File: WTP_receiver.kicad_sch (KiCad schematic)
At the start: 14 parts, among them J1 Conn_01x01_Male, J2 Conn_01x01_Male

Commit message: initial version with traces and components
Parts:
- added C10, C11, C12, C13, C14, C7, C8, C9: C, Capacitor_SMD:C_1111_2828_metric, symbol Device:C
- added C5: 10uF, Capacitor_SMD:C_1210_3225Metric, symbol Device:C
- added C6: 22uF, Capacitor_SMD:C_0603_1608Metric, symbol Device:C
- added P1: USB_C_Plug_USB2.0, Connector_USB:USB_C_Receptacle_GCT_USB4105-xx-A_16P_TopMnt_Horizontal, symbol Connector:USB_C_Plug_USB2.0
- added U1: ~, capacitor_bank:Capacitor bank, symbol extra_symbols:Capacitor_bank
- added U2: P7815-500R, P7815-500R:CONV_P7815-500R, symbol extra_symbols:P7815-500R
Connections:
- net AC1: now also C10.2, C11.1, C12.1, C13.1, C14.1, C7.2, C8.2, C9.2
- net GND: now also C5.2, C6.2, P1.A1 (GND), P1.A12 (GND), P1.B1 (GND), P1.B12 (GND), P1.S1 (SHIELD), U2.2 (GND)
- net AC2 renamed Coil2
- net DC+ renamed VDC
- net VDC: now also C5.1, U2.1 (+VIN)
- new net +5V: C6.1, P1.A4 (VBUS), P1.A9 (VBUS), P1.B4 (VBUS), P1.B9 (VBUS), U2.3 (+VO)
- new net Coil1: C10.1, C11.2, C12.2, C13.2, C14.2, C7.1, C8.1, C9.1
- no-connect marks 0 -> 4
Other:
- note added: "Capacitor bank"
- note added: "Linear regulator"
- note added: "To be ordered without any components attached will be tuned with the coil"
- note added: "USB-C Connector (Maybe?)"
- moved on the sheet: H1, H2, H3, H4

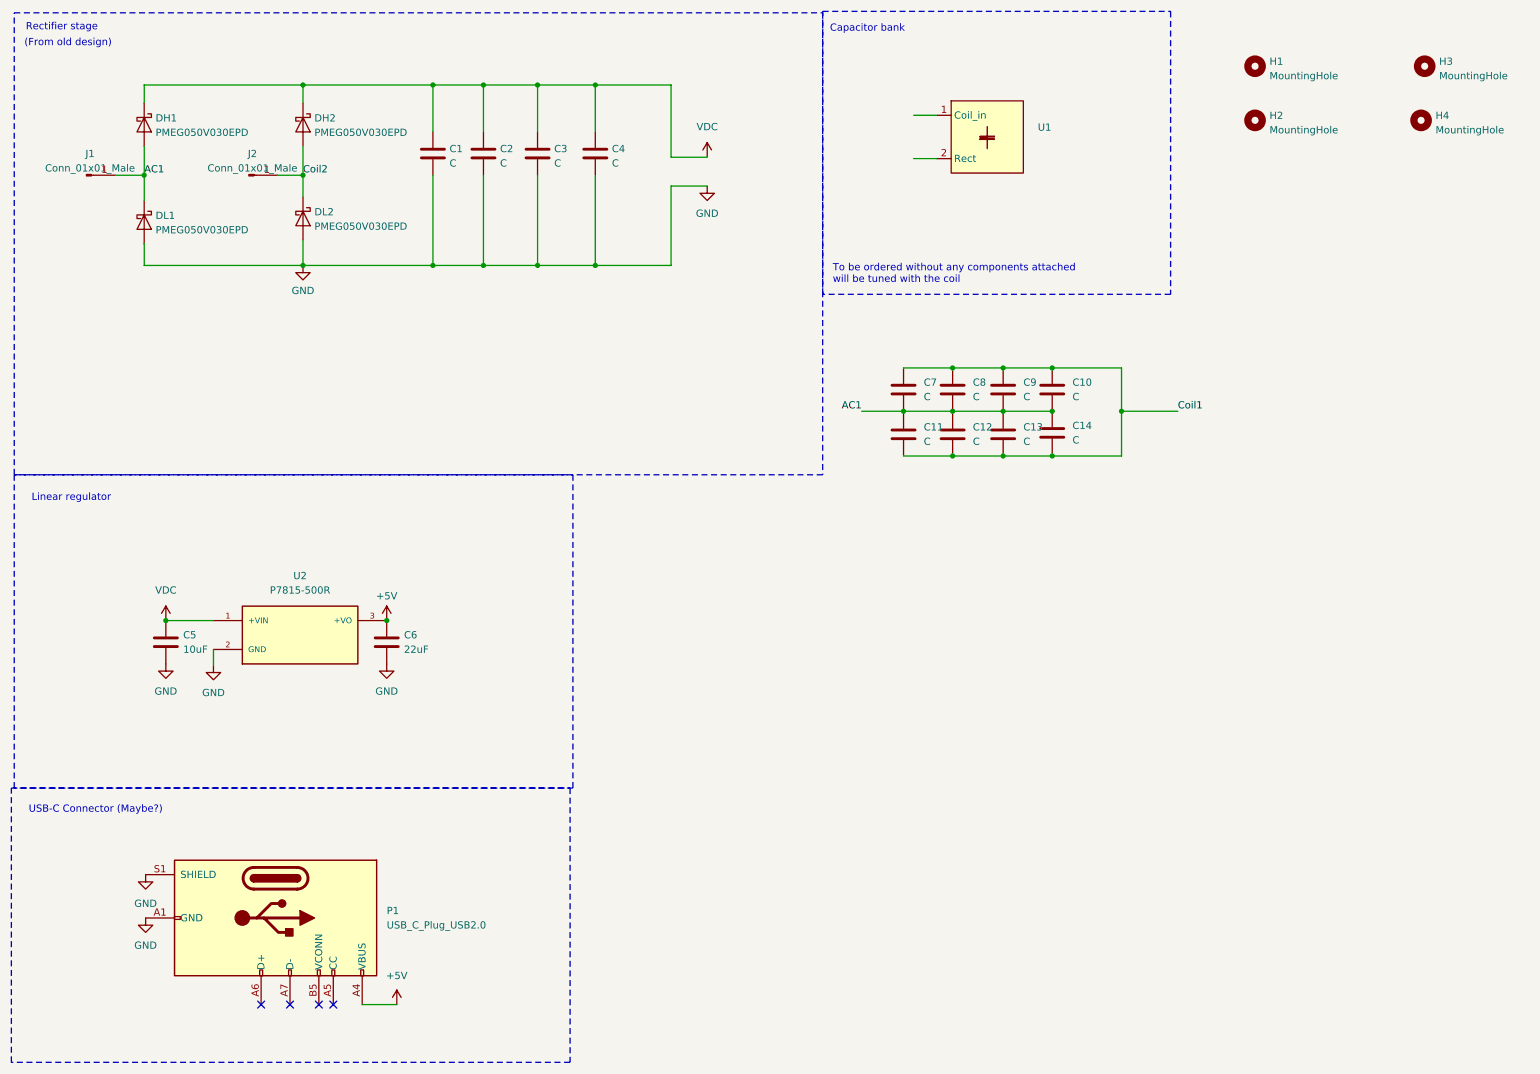
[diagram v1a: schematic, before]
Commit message: improvements done according to what was agreed in the project meeting
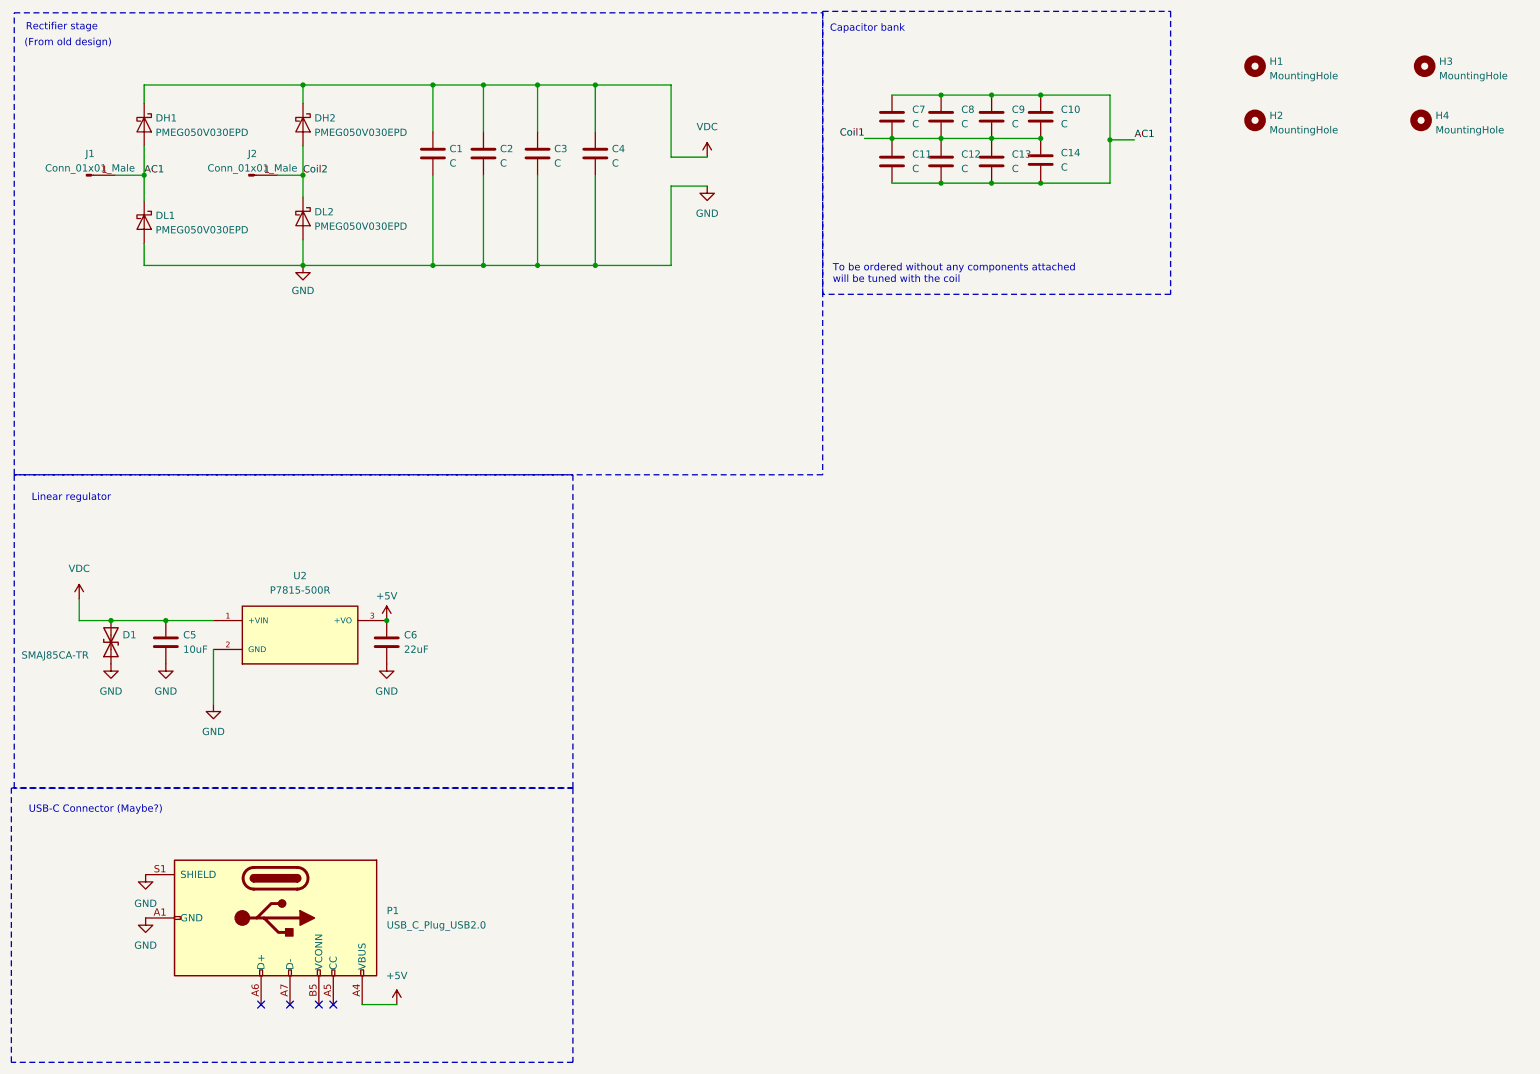
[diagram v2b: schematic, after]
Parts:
- removed U1: ~, capacitor_bank:Capacitor bank, symbol extra_symbols:Capacitor_bank
- added D1: SMAJ85CA-TR, Diode_SMD:D_SMA, symbol Device:D_TVS
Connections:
- net AC1: now also C10.1, C11.2, C12.2, C13.2, C14.2, C7.1, C8.1, C9.1; no longer C10.2, C11.1, C12.1, C13.1, C14.1, C7.2, C8.2, C9.2
- net Coil1: now also C10.2, C11.1, C12.1, C13.1, C14.1, C7.2, C8.2, C9.2; no longer C10.1, C11.2, C12.2, C13.2, C14.2, C7.1, C8.1, C9.1
- net GND: now also D1.1 (A1)
- net VDC: now also D1.2 (A2)
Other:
- moved on the sheet: C10, C11, C12, C13, C14, C7, C8, C9

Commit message: generate gerbers, start working with BOM
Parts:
- removed J1, J2: Conn_01x01_Male, TestPoint:TestPoint_Pad_4.0x4.0mm, symbol Connector:Conn_01x01_Male
- removed P1: USB_C_Plug_USB2.0, Connector_USB:USB_C_Receptacle_GCT_USB4105-xx-A_16P_TopMnt_Horizontal, symbol Connector:USB_C_Plug_USB2.0
- added J3: TYPE-C_16PIN_2MD__073_, components:SHOUHAN_TYPE-C_16PIN_2MD__073_, symbol TYPE-C_16PIN_2MD__073_:TYPE-C_16PIN_2MD__073_
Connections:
- net +5V: now also J3.A4_B9 (VBUS), J3.B4_A9 (VBUS)
- net GND: now also J3.A1_B12 (GND), J3.B1_A12 (GND), J3.SH1 (SHIELD), J3.SH2 (SHIELD), J3.SH3 (SHIELD), J3.SH4 (SHIELD)
- no-connect marks 4 -> 2

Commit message: update BOM and gerbers
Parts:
- C1, C10, C11, C12, C13, C14, C2, C3, C4, C7, C8, C9, D1, DH1, DH2, DL1, DL2, H1, H2, H3, H4, U2: JLCPCB BOM (none) -> 0
- C5: footprint Capacitor_SMD:C_1210_3225Metric -> Capacitor_SMD:C_2220_5650Metric; LCSC Part (none) -> C153035
- C6: footprint Capacitor_SMD:C_0603_1608Metric -> Capacitor_SMD:C_0805_2012Metric; LCSC Part (none) -> C5137600
- J3: LCSC Part (none) -> C668624
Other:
- note added: "Regulator and TVS to be soldered on site, capacitors installed by JLCPCB"
- note added: "To be assembled at JLCPCB"
- note added: "USB-C Connector"
- note removed: "USB-C Connector (Maybe?)"
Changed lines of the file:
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@@
     (effects (font (size 1.27 1.27)) (justify left bottom))
   )
-  (text "USB-C Connector (Maybe?)" (at 15.24 153.67 0)
+  (text "USB-C Connector " (at 15.24 153.67 0)
     (effects (font (size 1.27 1.27)) (justify left bottom))
   )
+  (text "To be assembled at JLCPCB" (at 15.24 192.024 0)
+    (effects (font (size 1.27 1.27)) (justify left bottom))
+  )
   (text "Rectifier stage" (at 14.732 16.002 0)
+    (effects (font (size 1.27 1.27)) (justify left bottom))
+  )
+  (text "Regulator and TVS to be soldered on site, capacitors installed by JLCPCB\n"
+    (at 15.748 145.542 0)
     (effects (font (size 1.27 1.27)) (justify left bottom))
   )
@@
     (property "SNAPEDA_PN" "TYPE-C 16PIN 2MD (073)" (at 59.436 171.45 0)
       (effects (font (size 1.27 1.27)) (justify bottom) hide)
+    )
+    (property "LCSC Part" "C668624" (at 59.436 171.45 0)
+      (effects (font (size 1.27 1.27)) hide)
     )
     (pin "A1_B12")
@@
       (effects (font (size 1.27 1.27)) hide)
     )
+    (property "JLCPCB BOM" "0" (at 231.013 31.623 0)
+      (effects (font (size 1.27 1.27)) hide)
+    )
     (instances
       (project ""
@@
       (effects (font (size 1.27 1.27)) hide)
     )
+    (property "JLCPCB BOM" "0" (at 104.775 37.465 0)
+      (effects (font (size 1.27 1.27)) hide)
+    )
+    (property "Field5" "" (at 104.775 37.465 0)
+      (effects (font (size 1.27 1.27)) hide)
+    )
     (pin "1")
     (pin "2")
@@
       (effects (font (size 1.27 1.27)) (justify left))
     )
-    (property "Footprint" "Capacitor_SMD:C_1210_3225Metric" (at 40.3352 127.254 0)
-      (effects (font (size 1.27 1.27)) hide)
-    )
-    (property "Datasheet" "~" (at 39.37 123.444 0)
+    (property "Footprint" "Capacitor_SMD:C_2220_5650Metric" (at 40.3352 127.254 0)
+      (effects (font (size 1.27 1.27)) hide)
+    )
+    (property "Datasheet" "https://jlcpcb.com/partdetail/164377-FS55X106K101EHG/C153035" (at 39.37 123.444 0)
+      (effects (font (size 1.27 1.27)) hide)
+    )
+    (property "LCSC Part" "C153035" (at 39.37 123.444 0)
       (effects (font (size 1.27 1.27)) hide)
     )
@@
     )
     (property "Datasheet" "~" (at 86.36 37.465 0)
+      (effects (font (size 1.27 1.27)) hide)
+    )
+    (property "JLCPCB BOM" "0" (at 86.36 37.465 0)
       (effects (font (size 1.27 1.27)) hide)
     )
@@
       (effects (font (size 1.27 1.27)) hide)
     )
+    (property "JLCPCB BOM" "0" (at 167.132 30.988 0)
+      (effects (font (size 1.27 1.27)) hide)
+    )
     (pin "1")
     (pin "2")
@@
     )
     (property "Datasheet" "~" (at 95.25 37.465 0)
+      (effects (font (size 1.27 1.27)) hide)
+    )
+    (property "JLCPCB BOM" "0" (at 95.25 37.465 0)
       (effects (font (size 1.27 1.27)) hide)
     )
@@
       (effects (font (size 1.27 1.27)) hide)
     )
+    (property "JLCPCB BOM" "0" (at 35.56 32.385 90)
+      (effects (font (size 1.27 1.27)) hide)
+    )
     (pin "1")
     (pin "2")
@@
       (effects (font (size 1.27 1.27)) (justify left))
     )
-    (property "Footprint" "Capacitor_SMD:C_0603_1608Metric" (at 79.1972 127.254 0)
-      (effects (font (size 1.27 1.27)) hide)
-    )
-    (property "Datasheet" "~" (at 78.232 123.444 0)
+    (property "Footprint" "Capacitor_SMD:C_0805_2012Metric" (at 79.1972 127.254 0)
+      (effects (font (size 1.27 1.27)) hide)
+    )
+    (property "Datasheet" "https://jlcpcb.com/partdetail/Fojan-FCC0805X226M100FT/C5137600" (at 78.232 123.444 0)
+      (effects (font (size 1.27 1.27)) hide)
+    )
+    (property "LCSC Part" "C5137600" (at 78.232 123.444 0)
       (effects (font (size 1.27 1.27)) hide)
     )
@@
       (effects (font (size 1.27 1.27)) (justify bottom) hide)
     )
+    (property "JLCPCB BOM" "0" (at 62.992 122.174 0)
+      (effects (font (size 1.27 1.27)) hide)
+    )
     (pin "1")
     (pin "2")
@@
     )
     (property "Datasheet" "https://assets.nexperia.com/documents/data-sheet/PMEG050V030EPD.pdf" (at 63.5 32.385 0)
+      (effects (font (size 1.27 1.27)) hide)
+    )
+    (property "JLCPCB BOM" "0" (at 63.5 32.385 90)
       (effects (font (size 1.27 1.27)) hide)
     )
@@
       (effects (font (size 1.27 1.27)) hide)
     )
+    (property "JLCPCB BOM" "0" (at 193.294 30.988 0)
+      (effects (font (size 1.27 1.27)) hide)
+    )
     (pin "1")
     (pin "2")
@@
     )
     (property "Datasheet" "https://assets.nexperia.com/documents/data-sheet/PMEG050V030EPD.pdf" (at 63.5 48.895 0)
+      (effects (font (size 1.27 1.27)) hide)
+    )
+    (property "JLCPCB BOM" "0" (at 63.5 48.895 90)
       (effects (font (size 1.27 1.27)) hide)
     )
@@
       (effects (font (size 1.27 1.27)) hide)
     )
+    (property "JLCPCB BOM" "0" (at 260.858 22.098 0)
+      (effects (font (size 1.27 1.27)) hide)
+    )
     (instances
       (project ""
@@
       (effects (font (size 1.27 1.27)) hide)
     )
+    (property "JLCPCB BOM" "0" (at 184.658 30.988 0)
+      (effects (font (size 1.27 1.27)) hide)
+    )
     (pin "1")
     (pin "2")
@@
     )
     (property "Datasheet" "https://assets.nexperia.com/documents/data-sheet/PMEG050V030EPD.pdf" (at 35.56 49.53 0)
+      (effects (font (size 1.27 1.27)) hide)
+    )
+    (property "JLCPCB BOM" "0" (at 35.56 49.53 90)
       (effects (font (size 1.27 1.27)) hide)
     )
@@
       (effects (font (size 1.27 1.27)) hide)
     )
+    (property "JLCPCB BOM" "0" (at 114.935 37.465 0)
+      (effects (font (size 1.27 1.27)) hide)
+    )
     (pin "1")
     (pin "2")
@@
       (effects (font (size 1.27 1.27)) hide)
     )
+    (property "JLCPCB BOM" "0" (at 175.768 30.988 0)
+      (effects (font (size 1.27 1.27)) hide)
+    )
     (pin "1")
     (pin "2")
@@
     )
     (property "Datasheet" "~" (at 175.768 38.862 0)
+      (effects (font (size 1.27 1.27)) hide)
+    )
+    (property "JLCPCB BOM" "0" (at 175.768 38.862 0)
       (effects (font (size 1.27 1.27)) hide)
     )
@@
       (effects (font (size 1.27 1.27)) hide)
     )
+    (property "JLCPCB BOM" "0" (at 29.718 123.444 90)
+      (effects (font (size 1.27 1.27)) hide)
+    )
     (pin "1")
     (pin "2")
@@
       (effects (font (size 1.27 1.27)) hide)
     )
+    (property "JLCPCB BOM" "0" (at 193.294 38.608 0)
+      (effects (font (size 1.27 1.27)) hide)
+    )
     (pin "1")
     (pin "2")
@@
       (effects (font (size 1.27 1.27)) hide)
     )
+    (property "JLCPCB BOM" "0" (at 167.132 38.862 0)
+      (effects (font (size 1.27 1.27)) hide)
+    )
     (pin "1")
     (pin "2")
@@
     )
     (property "Datasheet" "~" (at 260.223 31.623 0)
+      (effects (font (size 1.27 1.27)) hide)
+    )
+    (property "JLCPCB BOM" "0" (at 260.223 31.623 0)
       (effects (font (size 1.27 1.27)) hide)
     )
@@
       (effects (font (size 1.27 1.27)) hide)
     )
+    (property "JLCPCB BOM" "0" (at 231.013 22.098 0)
+      (effects (font (size 1.27 1.27)) hide)
+    )
     (instances
       (project ""
@@
       (effects (font (size 1.27 1.27)) hide)
     )
+    (property "JLCPCB BOM" "0" (at 184.658 38.862 0)
+      (effects (font (size 1.27 1.27)) hide)
+    )
